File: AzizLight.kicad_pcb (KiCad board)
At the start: 2 copper layers, 70.1 x 29.2 mm, 58 parts, among them P1 +9V, Q1 BS170, Q2 BS170, Q3 BS170, Q4 BS170, SW1 Reset, SW2 Invert, U1 MCP602, U2 LM393, U3 MCP601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

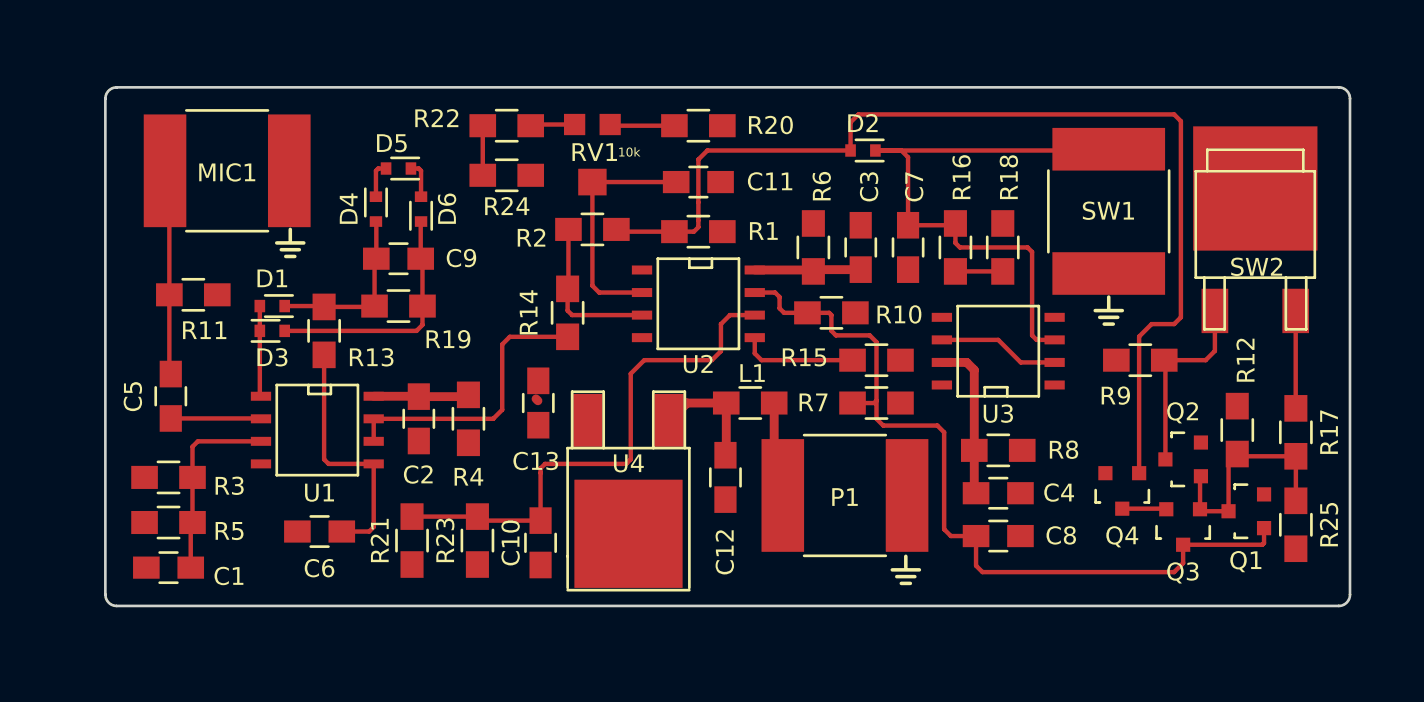
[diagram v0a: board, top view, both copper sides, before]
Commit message: PCB layout finished.
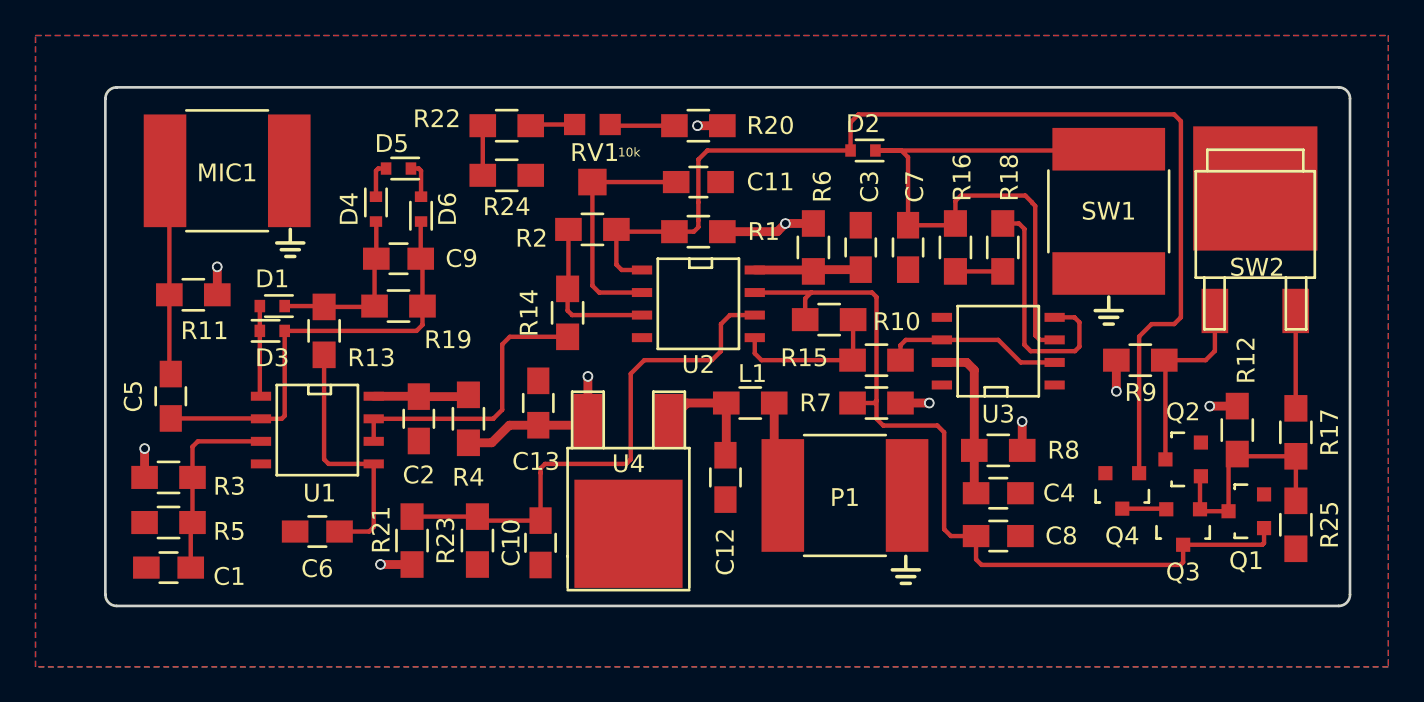
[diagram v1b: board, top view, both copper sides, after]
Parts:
- moved R10 0.40 mm to (156.5, 89.7)
- moved C6 0.13 mm to (127.6, 101.6)
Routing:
- net +5V: track 0.00 -> 28.0 mm, vias 0 -> 10
- net GND: track 0.00 -> 14.1 mm
- net Net-(C5-Pad1): track 18.9 -> 25.1 mm
- net Net-(D2-Pad2): track 59.4 -> 63.0 mm
- net Net-(R15-Pad2): track 6.88 -> 10.2 mm
- net Net-(C7-Pad1): track 33.4 -> 36.3 mm
- net Net-(R10-Pad2): track 6.55 -> 8.85 mm
- net Net-(C8-Pad1): track 46.3 -> 48.0 mm
- added copper zone on B.Cu, net +5V
- added copper zone on F.Cu, net GND
